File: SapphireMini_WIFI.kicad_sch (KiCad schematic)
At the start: 6 parts, among them M701 AdafruitWINC1500

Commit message: Corrected to get clean review on schematic
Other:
- company: Southern Methodist Univ -> (none)
- title: Sapphire Mini M2 -> (none)
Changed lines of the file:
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@@
 (kicad_sch (version 20211123) (generator eeschema)
   (paper "A4")
-  (title_block
-    (title "Sapphire Mini M2")
-    (date "2022-09-26")
-    (rev "1")
-    (company "Southern Methodist Univ")
-    (comment 1 "Chris Hayward")
-  )
   (junction (at 154.94 45.72) (diameter 0) (color 0 0 0 0)
   )
@@
   (symbol (lib_id "power:GND") (at 125.73 54.61 0) (unit 1)
     (in_bom yes) (on_board yes)
-    (property "Reference" "#PWR0701" (id 0) (at 125.73 60.96 0)
+    (property "Reference" "#PWR?" (id 0) (at 125.73 60.96 0)
       (effects (font (size 1.27 1.27)) hide)
     )
@@
   (symbol (lib_id "power:GND") (at 149.86 54.61 0) (unit 1)
     (in_bom yes) (on_board yes)
-    (property "Reference" "#PWR0702" (id 0) (at 149.86 60.96 0)
-      (effects (font (size 1.27 1.27)) hide)
-    )
+    (property "Reference" "#PWR?" (id 0) (at 149.86 60.96 0)
+      (effects (font (size 1.27 1.27)) hide)
+    )

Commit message: daily update
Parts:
- added R702, R703: 47, Resistor_SMD:R_0603_1608Metric, symbol Device:R_US
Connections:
- net SPI_MOSI: now also R703.2; no longer M701.5 (MOSI)
- net SPI_SCK: now also R702.2; no longer M701.3 (SCK)
- new net: M701.3 (SCK), R702.1
- new net: M701.5 (MOSI), R703.1
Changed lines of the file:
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@@
+    (stroke (width 0) (type default) (color 0 0 0 0))
+  )
+  (wire (pts (xy 151.13 76.2) (xy 134.62 76.2))
+    (stroke (width 0) (type default) (color 0 0 0 0))
+  )
+  (wire (pts (xy 151.13 71.12) (xy 134.62 71.12))
     (stroke (width 0) (type default) (color 0 0 0 0))
   )
@@
     (stroke (width 0) (type default) (color 0 0 0 0))
   )
-  (wire (pts (xy 165.1 71.12) (xy 134.62 71.12))
+  (wire (pts (xy 165.1 71.12) (xy 158.75 71.12))
     (stroke (width 0) (type default) (color 0 0 0 0))
   )
@@
     (stroke (width 0) (type default) (color 0 0 0 0))
   )
-  (wire (pts (xy 165.1 76.2) (xy 134.62 76.2))
+  (wire (pts (xy 165.1 76.2) (xy 158.75 76.2))
     (stroke (width 0) (type default) (color 0 0 0 0))
   )
@@
       (effects (font (size 1.27 1.27)) hide)
     )
+    (pin "1")
+    (pin "2")
+  )
+  (symbol (lib_id "Device:R_US") (at 154.94 76.2 270) (unit 1)
+    (in_bom yes) (on_board yes)
+    (property "Reference" "R703" (id 0) (at 151.13 74.93 90))
+    (property "Value" "47" (id 1) (at 157.48 74.93 90))
+    (property "Footprint" "Resistor_SMD:R_0603_1608Metric" (id 2) (at 154.686 77.216 90)
+      (effects (font (size 1.27 1.27)) hide)
+    )
+    (property "Datasheet" "~" (id 3) (at 154.94 76.2 0)
+      (effects (font (size 1.27 1.27)) hide)
+    )
+    (pin "1")
+    (pin "2")
+  )
+  (symbol (lib_id "Device:R_US") (at 154.94 71.12 270) (unit 1)
+    (in_bom yes) (on_board yes)
+    (property "Reference" "R702" (id 0) (at 151.13 69.85 90))
+    (property "Value" "47" (id 1) (at 157.48 69.85 90))
+    (property "Footprint" "Resistor_SMD:R_0603_1608Metric" (id 2) (at 154.686 72.136 90)
+      (effects (font (size 1.27 1.27)) hide)
+    )
+    (property "Datasheet" "~" (id 3) (at 154.94 71.12 0)
+      (effects (font (size 1.27 1.27)) hide)
+    )

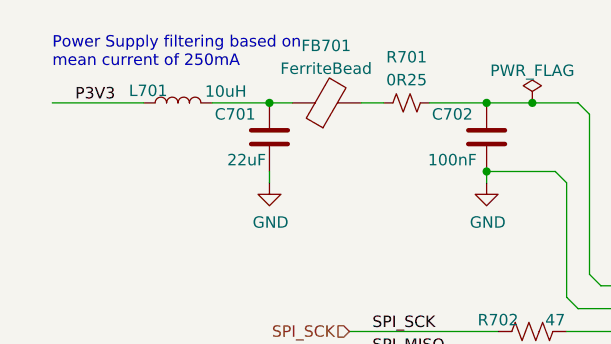
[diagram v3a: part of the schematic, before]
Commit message: Footprints complete. Starting layout
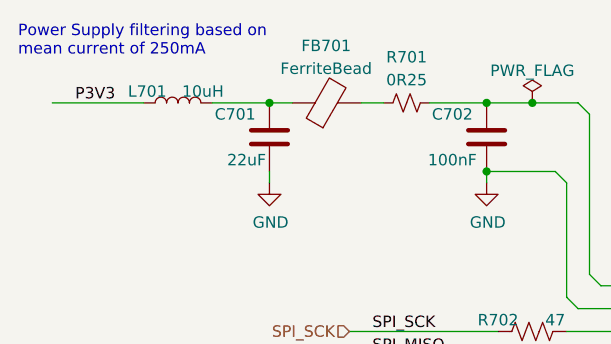
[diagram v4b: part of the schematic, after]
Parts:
- C701: MPN (none) -> CL21A226MAYNNNE; Manufacturer (none) -> Samsung; Populate (none) -> 1
- C702: MPN (none) -> CL05A104KA5NNNC; Manufacturer (none) -> Samsung; Populate (none) -> 1
- FB701: footprint (none) -> Inductor_SMD:L_0201_0603Metric; MPN (none) -> BLM18AG221SN1D
- L701: footprint (none) -> SapphineMinimal:NR3012T100M; MPN (none) -> NR3012T100M; Manufacturer (none) -> Taiyo Yuden
- M701: footprint (none) -> Connector_PinHeader_2.54mm:PinHeader_1x13_P2.54mm_Vertical
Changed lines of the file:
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@@
   )
   (text "Power Supply filtering based on\nmean current of 250mA"
-    (at 101.6 41.91 0)
+    (at 97.79 40.64 0)
     (effects (font (size 1.27 1.27)) (justify left bottom))
   )
@@
       (effects (font (size 1.27 1.27)) (justify left))
     )
-    (property "Footprint" "" (id 2) (at 170.18 66.04 0)
+    (property "Footprint" "Connector_PinHeader_2.54mm:PinHeader_1x13_P2.54mm_Vertical" (id 2) (at 170.18 66.04 0)
       (effects (font (size 1.27 1.27)) hide)
     )
     (property "Datasheet" "" (id 3) (at 170.18 66.04 0)
+      (effects (font (size 1.27 1.27)) hide)
+    )
+    (property "Description" "Adafruit Winc1500 breakout" (id 4) (at 170.18 66.04 0)
       (effects (font (size 1.27 1.27)) hide)
     )
@@
     (pin "9")
   )
-  (symbol (lib_id "Device:L") (at 115.57 45.72 90) (unit 1)
-    (in_bom yes) (on_board yes)
-    (property "Reference" "L701" (id 0) (at 114.4016 44.3738 90)
-      (effects (font (size 1.27 1.27)) (justify left))
-    )
-    (property "Value" "10uH" (id 1) (at 123.19 44.45 90)
-      (effects (font (size 1.27 1.27)) (justify left))
-    )
-    (property "Footprint" "" (id 2) (at 115.57 45.72 0)
-      (effects (font (size 1.27 1.27)) hide)
-    )
-    (property "Datasheet" "~" (id 3) (at 115.57 45.72 0)
-      (effects (font (size 1.27 1.27)) hide)
-    )
-    (pin "1")
-    (pin "2")
-  )
   (symbol (lib_id "Device:C") (at 149.86 49.53 0) (unit 1)
     (in_bom yes) (on_board yes)
@@
       (effects (font (size 1.27 1.27)) hide)
     )
+    (property "Description" "0.1 µF ±10% 25V Ceramic Capacitor X5R 0402 (1005 Metric)" (id 4) (at 149.86 49.53 0)
+      (effects (font (size 1.27 1.27)) hide)
+    )
+    (property "MPN" "CL05A104KA5NNNC" (id 5) (at 149.86 49.53 0)
+      (effects (font (size 1.27 1.27)) hide)
+    )
+    (property "Manufacturer" "Samsung" (id 6) (at 149.86 49.53 0)
+      (effects (font (size 1.27 1.27)) hide)
+    )
+    (property "Populate" "1" (id 7) (at 149.86 49.53 0)
+      (effects (font (size 1.27 1.27)) hide)
+    )
     (pin "1")
     (pin "2")
@@
     )
     (property "Datasheet" "~" (id 3) (at 125.73 49.53 0)
+      (effects (font (size 1.27 1.27)) hide)
+    )
+    (property "Description" "22 µF ±20% 25V Ceramic Capacitor X5R 0805 (2012 Metric)" (id 4) (at 125.73 49.53 0)
+      (effects (font (size 1.27 1.27)) hide)
+    )
+    (property "MPN" "CL21A226MAYNNNE" (id 5) (at 125.73 49.53 0)
+      (effects (font (size 1.27 1.27)) hide)
+    )
+    (property "Manufacturer" "Samsung" (id 6) (at 125.73 49.53 0)
+      (effects (font (size 1.27 1.27)) hide)
+    )
+    (property "Populate" "1" (id 7) (at 125.73 49.53 0)
       (effects (font (size 1.27 1.27)) hide)
     )
@@
     (property "Reference" "FB701" (id 0) (at 132.0292 39.3786 90))
     (property "Value" "FerriteBead" (id 1) (at 132.0292 41.9155 90))
-    (property "Footprint" "" (id 2) (at 132.08 47.498 90)
+    (property "Footprint" "Inductor_SMD:L_0201_0603Metric" (id 2) (at 132.08 47.498 90)
       (effects (font (size 1.27 1.27)) hide)
     )
@@
       (effects (font (size 1.27 1.27)) hide)
     )
+    (property "Description" "220 Ohms @ 100 MHz 1 Ferrite Bead 0603 (1608 Metric) 500mA 250mOhm" (id 4) (at 132.08 45.72 0)
+      (effects (font (size 1.27 1.27)) hide)
+    )
+    (property "MPN" "BLM18AG221SN1D" (id 5) (at 132.08 45.72 0)
+      (effects (font (size 1.27 1.27)) hide)
+    )
+    (pin "1")
+    (pin "2")
+  )
+  (symbol (lib_id "Device:L") (at 115.57 45.72 90) (unit 1)
+    (in_bom yes) (on_board yes)
+    (property "Reference" "L701" (id 0) (at 114.3 44.45 90)
+      (effects (font (size 1.27 1.27)) (justify left))
+    )
+    (property "Value" "10uH" (id 1) (at 120.65 44.45 90)
+      (effects (font (size 1.27 1.27)) (justify left))
+    )
+    (property "Footprint" "SapphineMinimal:NR3012T100M" (id 2) (at 115.57 45.72 0)
+      (effects (font (size 1.27 1.27)) hide)
+    )
+    (property "Datasheet" "~" (id 3) (at 115.57 45.72 0)
+      (effects (font (size 1.27 1.27)) hide)
+    )
+    (property "Description" "FIXED IND 10UH 630MA 348MOHM SMD" (id 4) (at 115.57 45.72 0)
+      (effects (font (size 1.27 1.27)) hide)
+    )
+    (property "MPN" "NR3012T100M" (id 5) (at 115.57 45.72 0)
+      (effects (font (size 1.27 1.27)) hide)
+    )
+    (property "Manufacturer" "Taiyo Yuden" (id 6) (at 115.57 45.72 0)
+      (effects (font (size 1.27 1.27)) hide)
+    )

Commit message: Working on update to power controllers
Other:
- company: (none) -> Southern Methodist Univ
- title: (none) -> Sapphire Mini M2
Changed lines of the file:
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@@
 (kicad_sch (version 20211123) (generator eeschema)
   (paper "A4")
+  (title_block
+    (title "Sapphire Mini M2")
+    (date "2022-09-26")
+    (rev "1")
+    (company "Southern Methodist Univ")
+    (comment 1 "Chris Hayward")
+  )
   (junction (at 154.94 45.72) (diameter 0) (color 0 0 0 0)
   )

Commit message: Checkpoint
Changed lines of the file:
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@@
     (effects (font (size 1.27 1.27)) (justify left bottom))
+  )
+  (hierarchical_label "P3V3" (shape input) (at 101.6 45.72 180)
+    (effects (font (size 1.27 1.27)) (justify right))
   )
   (hierarchical_label "WIFI_IRQ" (shape output) (at 134.62 83.82 180)

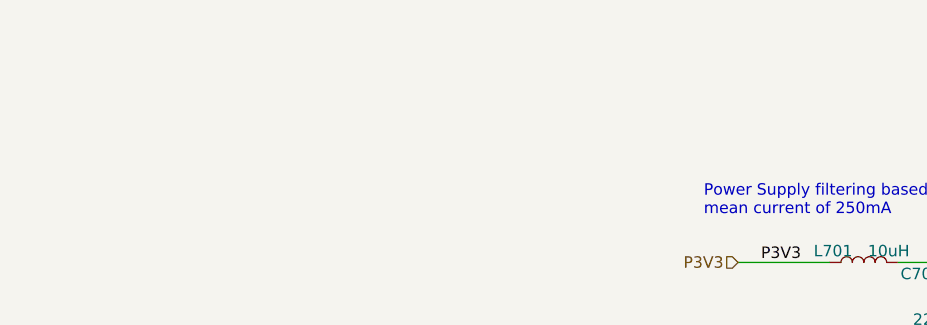
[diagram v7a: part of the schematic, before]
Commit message: Updating for parts avail
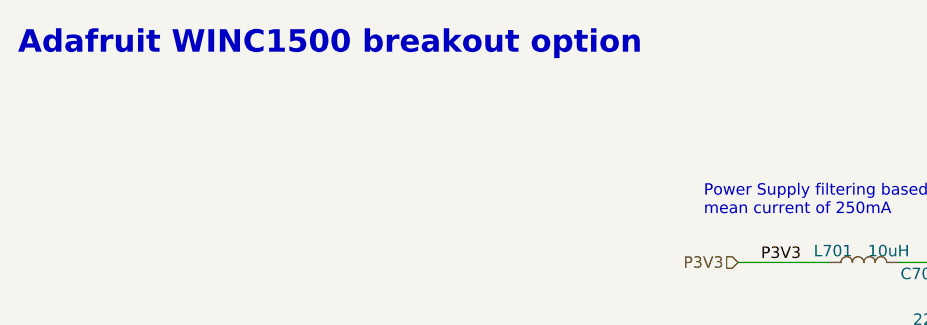
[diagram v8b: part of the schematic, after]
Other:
- note added: "Adafruit WINC1500 breakout option"
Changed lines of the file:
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@@
 (kicad_sch (version 20211123) (generator eeschema)
-  (paper "A4")
+  (paper "A")
   (title_block
     (title "Sapphire Mini M2")
-    (date "2022-09-26")
+    (date "2022-10-04")
     (rev "1")
     (company "Southern Methodist Univ")
     (comment 1 "Chris Hayward")
+    (comment 2 "Markup copy w/ errors!")
   )
   (junction (at 154.94 45.72) (diameter 0) (color 0 0 0 0)
@@
     (stroke (width 0) (type default) (color 0 0 0 0))
   )
+  (text "Adafruit WINC1500 breakout option" (at 21.59 22.86 0)
+    (effects (font (size 2.5 2.5) (thickness 0.5) bold) (justify left bottom))
+  )
   (text "Pins 10-13 are not usable w/\ncurrent Adafruit Library"
